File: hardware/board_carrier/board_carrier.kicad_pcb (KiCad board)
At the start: 2 copper layers, 40 x 51.5 mm, 44 parts, among them J3 Conn_02x06_Top_Bottom, U1 TJA1051T-3, U2 LM78M05_TO252, U3 f042_wideband_module, U4 74LVC1G125, U5 REF3030, U6 LM2904

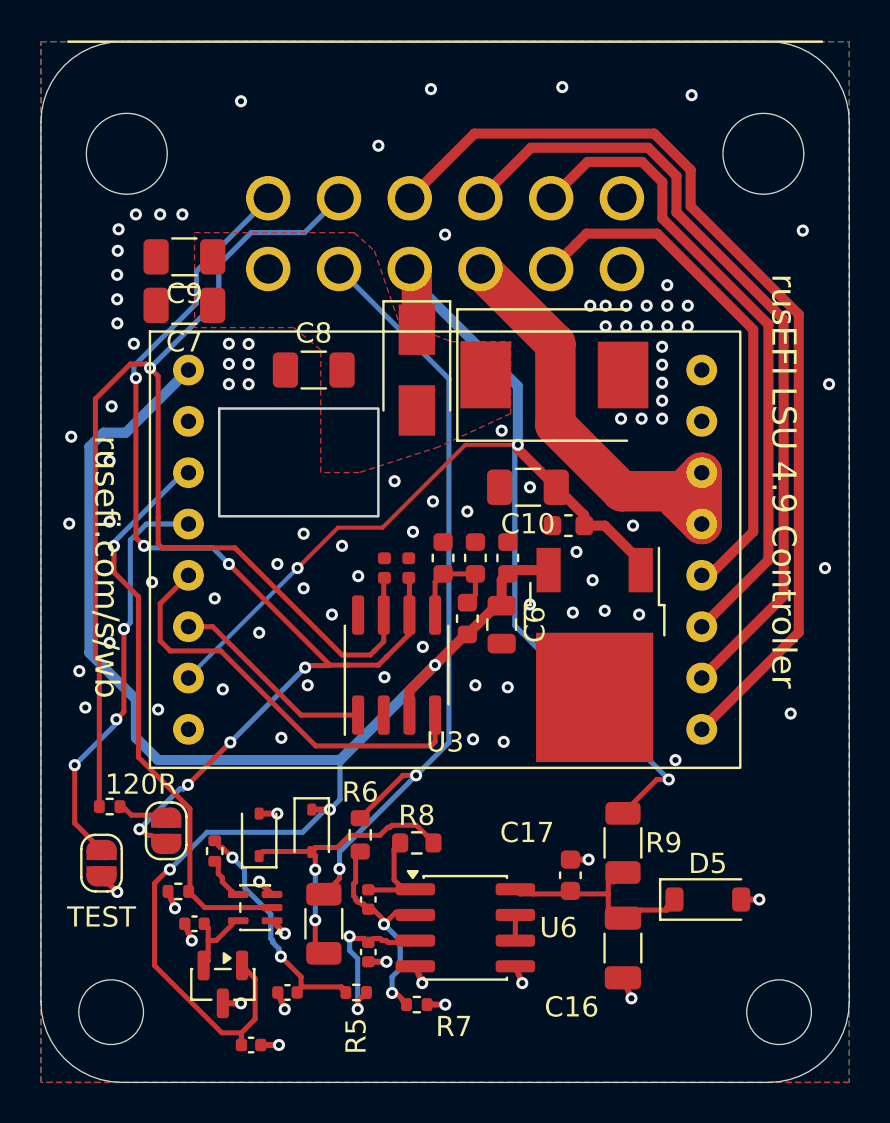
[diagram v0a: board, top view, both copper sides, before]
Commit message: board_carrier: r41: copper keep-out 3.6 mm around the mounting holes, both layers (pour was 0.3 mm from them). work: A3 expectation after the feedback move
Co-Authored-By: Claude Opus 5.5 <noreply@anthropic.com>
Claude-Session: https://claude.ai/code/session_013ZVt2aLpmrSY8uzxABcZfb
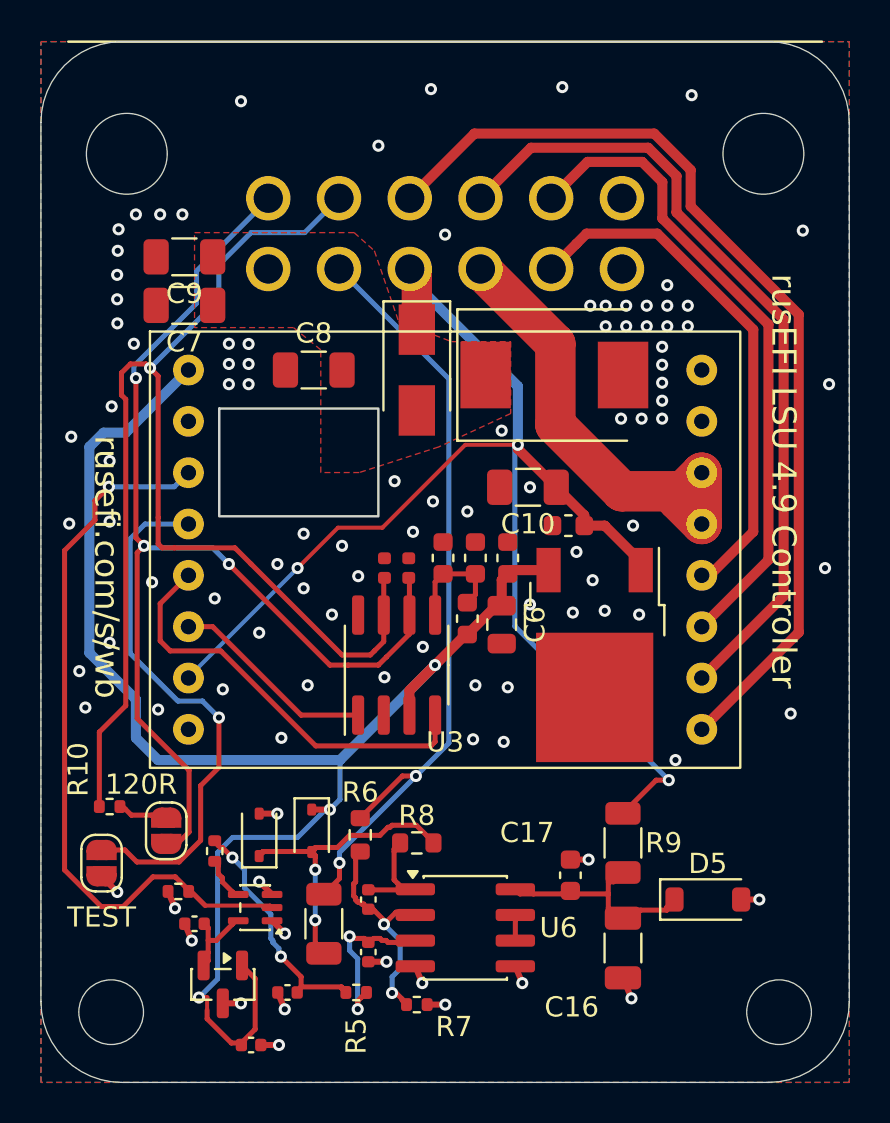
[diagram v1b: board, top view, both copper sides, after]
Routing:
- net /AOUT_PWM: track 28.4 -> 36.4 mm
- net /TEST_SEL2: track 20.2 -> 26.6 mm, vias 3 -> 1
- net /CAN_L: track 52.7 -> 55.9 mm, vias 7 -> 3
- net +5V: track 78.3 -> 76.0 mm

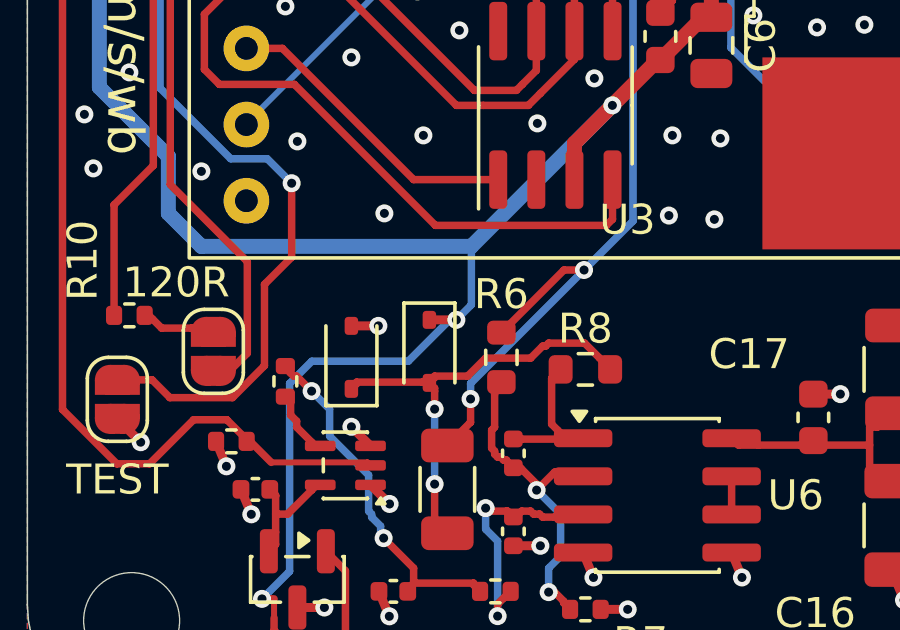
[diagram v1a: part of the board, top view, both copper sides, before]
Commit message: board_carrier, firmware: output low from reset (outside review B1): R3 100k -> 4.7k (C25900, Basic) and PB1 pull-down in the app and bootloader board.h; invalid lambda -> 5.0 V (N1, fail lean so a closed-loop ECU adds fuel). New checks: boot_level.py; sim/full_scale_corners.sh (clamps, R9 supply, +5V tolerance; R1). EasyEDA fetch through curl (urllib now 403)
Layout unchanged (0 parts moved, same tracks and vias); 23 checks, 0 failed, 2 advisory.

Co-Authored-By: Claude Opus 5.5 <noreply@anthropic.com>
Claude-Session: https://claude.ai/code/session_013ZVt2aLpmrSY8uzxABcZfb
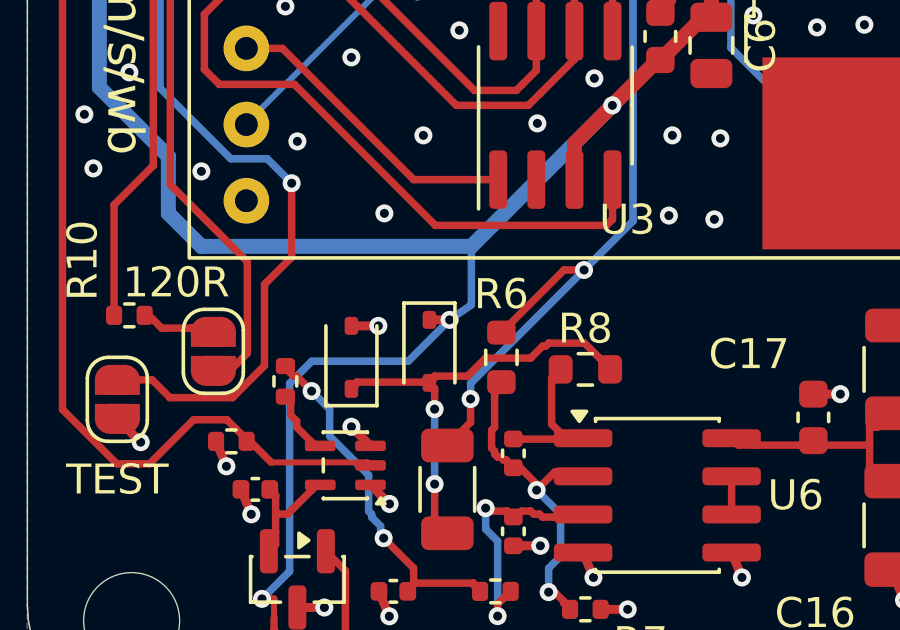
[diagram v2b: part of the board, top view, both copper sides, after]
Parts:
- R3: value 100k -> 4.7k

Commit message: board_carrier: J3 bottom labels: OUT (J3-5), GND (J3-7), and upstream's 12V under J3-6 restored (deleted since r1). work: docs/wiring.md (J3, sensor plug, SWD); SWD pad diagram from the board files (gen/swd_diagram.py), J2 fits the carrier cutout with ~1 mm each side; mating plug Molex 36792-1201; flash package built and checked at ba01449
DRC delta 0/0; 24 checks, 0 failed, 2 advisory.

Co-Authored-By: Claude Opus 5.5 <noreply@anthropic.com>
Claude-Session: https://claude.ai/code/session_013ZVt2aLpmrSY8uzxABcZfb
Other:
- board text added: "12V"
- board text added: "OUT"
